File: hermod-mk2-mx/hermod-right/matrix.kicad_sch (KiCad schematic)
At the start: 84 parts

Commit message: UPdated Hermod Mk 2 to have ks33 and choc v2 footprints
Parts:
- CH1, CH10, CH11, CH12, CH13, CH15, CH16, CH17, CH18, CH19, CH2, CH20, CH22, CH23, CH24, CH25, CH26, CH27, CH29, CH3, CH30, CH31, CH32, CH33, CH34, CH39, CH4, CH40, CH41, CH42, CH5, CH6, CH8, CH9: footprint Gateron_KS33_Hotswap:Gateron-KS33-Hotswap-1U -> ModHob:KS33_Choc-v2_HS_1U
- CH14, CH21, CH28, CH35, CH36, CH37, CH38, CH7: footprint Gateron_KS33_Hotswap:Gateron-KS33-Hotswap-1.5U -> ModHob:KS33_Choc-v2_HS_1.5U
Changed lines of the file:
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@@
 			)
 		)
-		(property "Footprint" "Gateron_KS33_Hotswap:Gateron-KS33-Hotswap-1.5U"
+		(property "Footprint" "ModHob:KS33_Choc-v2_HS_1.5U"
 			(at 247.65 162.56 0)
 			(effects
@@
 			)
 		)
-		(property "Footprint" "Gateron_KS33_Hotswap:Gateron-KS33-Hotswap-1U"
+		(property "Footprint" "ModHob:KS33_Choc-v2_HS_1U"
 			(at 212.09 186.69 0)
 			(effects
@@
 			)
 		)
-		(property "Footprint" "Gateron_KS33_Hotswap:Gateron-KS33-Hotswap-1U"
+		(property "Footprint" "ModHob:KS33_Choc-v2_HS_1U"
 			(at 229.87 186.69 0)
 			(effects
@@
 			)
 		)
-		(property "Footprint" "Gateron_KS33_Hotswap:Gateron-KS33-Hotswap-1U"
+		(property "Footprint" "ModHob:KS33_Choc-v2_HS_1U"
 			(at 158.75 95.25 0)
 			(effects
@@
 			)
 		)
-		(property "Footprint" "Gateron_KS33_Hotswap:Gateron-KS33-Hotswap-1U"
+		(property "Footprint" "ModHob:KS33_Choc-v2_HS_1U"
 			(at 212.09 118.11 0)
 			(effects
@@
 			)
 		)
-		(property "Footprint" "Gateron_KS33_Hotswap:Gateron-KS33-Hotswap-1U"
+		(property "Footprint" "ModHob:KS33_Choc-v2_HS_1U"
 			(at 229.87 95.25 0)
 			(effects
@@
 			)
 		)
-		(property "Footprint" "Gateron_KS33_Hotswap:Gateron-KS33-Hotswap-1U"
+		(property "Footprint" "ModHob:KS33_Choc-v2_HS_1U"
 			(at 158.75 139.7 0)
 			(effects
@@
 			)
 		)
-		(property "Footprint" "Gateron_KS33_Hotswap:Gateron-KS33-Hotswap-1U"
+		(property "Footprint" "ModHob:KS33_Choc-v2_HS_1U"
 			(at 158.75 162.56 0)
 			(effects
@@
 			)
 		)
-		(property "Footprint" "Gateron_KS33_Hotswap:Gateron-KS33-Hotswap-1U"
+		(property "Footprint" "ModHob:KS33_Choc-v2_HS_1U"
 			(at 194.31 72.39 0)
 			(effects
@@
 			)
 		)
-		(property "Footprint" "Gateron_KS33_Hotswap:Gateron-KS33-Hotswap-1U"
+		(property "Footprint" "ModHob:KS33_Choc-v2_HS_1U"
 			(at 140.97 139.7 0)
 			(effects
@@
 			)
 		)
-		(property "Footprint" "Gateron_KS33_Hotswap:Gateron-KS33-Hotswap-1.5U"
+		(property "Footprint" "ModHob:KS33_Choc-v2_HS_1.5U"
 			(at 247.65 118.11 0)
 			(effects
@@
 			)
 		)
-		(property "Footprint" "Gateron_KS33_Hotswap:Gateron-KS33-Hotswap-1U"
+		(property "Footprint" "ModHob:KS33_Choc-v2_HS_1U"
 			(at 176.53 139.7 0)
 			(effects
@@
 			)
 		)
-		(property "Footprint" "Gateron_KS33_Hotswap:Gateron-KS33-Hotswap-1U"
+		(property "Footprint" "ModHob:KS33_Choc-v2_HS_1U"
 			(at 229.87 162.56 0)
 			(effects
@@
 			)
 		)
-		(property "Footprint" "Gateron_KS33_Hotswap:Gateron-KS33-Hotswap-1U"
+		(property "Footprint" "ModHob:KS33_Choc-v2_HS_1U"
 			(at 158.75 118.11 0)
 			(effects
@@
 			)
 		)
-		(property "Footprint" "Gateron_KS33_Hotswap:Gateron-KS33-Hotswap-1U"
+		(property "Footprint" "ModHob:KS33_Choc-v2_HS_1U"
 			(at 140.97 162.56 0)
 			(effects
@@
 			)
 		)
-		(property "Footprint" "Gateron_KS33_Hotswap:Gateron-KS33-Hotswap-1U"
+		(property "Footprint" "ModHob:KS33_Choc-v2_HS_1U"
 			(at 229.87 72.39 0)
 			(effects
@@
 			)
 		)
-		(property "Footprint" "Gateron_KS33_Hotswap:Gateron-KS33-Hotswap-1.5U"
+		(property "Footprint" "ModHob:KS33_Choc-v2_HS_1.5U"
 			(at 176.53 186.69 0)
 			(effects
@@
 			)
 		)
-		(property "Footprint" "Gateron_KS33_Hotswap:Gateron-KS33-Hotswap-1.5U"
+		(property "Footprint" "ModHob:KS33_Choc-v2_HS_1.5U"
 			(at 247.65 72.39 0)
 			(effects
@@
 			)
 		)
-		(property "Footprint" "Gateron_KS33_Hotswap:Gateron-KS33-Hotswap-1.5U"
+		(property "Footprint" "ModHob:KS33_Choc-v2_HS_1.5U"
 			(at 140.97 186.69 0)
 			(effects
@@
 			)
 		)
-		(property "Footprint" "Gateron_KS33_Hotswap:Gateron-KS33-Hotswap-1U"
+		(property "Footprint" "ModHob:KS33_Choc-v2_HS_1U"
 			(at 176.53 118.11 0)
 			(effects
@@
 			)
 		)
-		(property "Footprint" "Gateron_KS33_Hotswap:Gateron-KS33-Hotswap-1U"
+		(property "Footprint" "ModHob:KS33_Choc-v2_HS_1U"
 			(at 140.97 72.39 0)
 			(effects
@@
 			)
 		)
-		(property "Footprint" "Gateron_KS33_Hotswap:Gateron-KS33-Hotswap-1U"
+		(property "Footprint" "ModHob:KS33_Choc-v2_HS_1U"
 			(at 194.31 162.56 0)
 			(effects
@@
 			)
 		)
-		(property "Footprint" "Gateron_KS33_Hotswap:Gateron-KS33-Hotswap-1U"
+		(property "Footprint" "ModHob:KS33_Choc-v2_HS_1U"
 			(at 194.31 118.11 0)
 			(effects
@@
 			)
 		)
-		(property "Footprint" "Gateron_KS33_Hotswap:Gateron-KS33-Hotswap-1U"
+		(property "Footprint" "ModHob:KS33_Choc-v2_HS_1U"
 			(at 176.53 95.25 0)
 			(effects
@@
 			)
 		)
-		(property "Footprint" "Gateron_KS33_Hotswap:Gateron-KS33-Hotswap-1U"
+		(property "Footprint" "ModHob:KS33_Choc-v2_HS_1U"
 			(at 229.87 139.7 0)
 			(effects
@@
 			)
 		)
-		(property "Footprint" "Gateron_KS33_Hotswap:Gateron-KS33-Hotswap-1U"
+		(property "Footprint" "ModHob:KS33_Choc-v2_HS_1U"
 			(at 194.31 139.7 0)
 			(effects
@@
 			)
 		)
-		(property "Footprint" "Gateron_KS33_Hotswap:Gateron-KS33-Hotswap-1U"
+		(property "Footprint" "ModHob:KS33_Choc-v2_HS_1U"
 			(at 140.97 95.25 0)
 			(effects
@@
 			)
 		)
-		(property "Footprint" "Gateron_KS33_Hotswap:Gateron-KS33-Hotswap-1U"
+		(property "Footprint" "ModHob:KS33_Choc-v2_HS_1U"
 			(at 158.75 72.39 0)
 			(effects
@@
 			)
 		)
-		(property "Footprint" "Gateron_KS33_Hotswap:Gateron-KS33-Hotswap-1U"
+		(property "Footprint" "ModHob:KS33_Choc-v2_HS_1U"
 			(at 229.87 118.11 0)
 			(effects
@@
 			)
 		)
-		(property "Footprint" "Gateron_KS33_Hotswap:Gateron-KS33-Hotswap-1U"
+		(property "Footprint" "ModHob:KS33_Choc-v2_HS_1U"
 			(at 212.09 72.39 0)
 			(effects
@@
 			)
 		)
-		(property "Footprint" "Gateron_KS33_Hotswap:Gateron-KS33-Hotswap-1.5U"
+		(property "Footprint" "ModHob:KS33_Choc-v2_HS_1.5U"
 			(at 158.75 186.69 0)
 			(effects
@@
 			)
 		)
-		(property "Footprint" "Gateron_KS33_Hotswap:Gateron-KS33-Hotswap-1.5U"
+		(property "Footprint" "ModHob:KS33_Choc-v2_HS_1.5U"
 			(at 247.65 139.7 0)
 			(effects
@@
 			)
 		)
-		(property "Footprint" "Gateron_KS33_Hotswap:Gateron-KS33-Hotswap-1U"
+		(property "Footprint" "ModHob:KS33_Choc-v2_HS_1U"
 			(at 140.97 118.11 0)
 			(effects
@@
 			)
 		)
-		(property "Footprint" "Gateron_KS33_Hotswap:Gateron-KS33-Hotswap-1U"
+		(property "Footprint" "ModHob:KS33_Choc-v2_HS_1U"
 			(at 212.09 162.56 0)
 			(effects
@@
 			)
 		)
-		(property "Footprint" "Gateron_KS33_Hotswap:Gateron-KS33-Hotswap-1U"
+		(property "Footprint" "ModHob:KS33_Choc-v2_HS_1U"
 			(at 247.65 186.69 0)
 			(effects
@@
 			)
 		)
-		(property "Footprint" "Gateron_KS33_Hotswap:Gateron-KS33-Hotswap-1U"
+		(property "Footprint" "ModHob:KS33_Choc-v2_HS_1U"
 			(at 176.53 72.39 0)
 			(effects
@@
 			)
 		)
-		(property "Footprint" "Gateron_KS33_Hotswap:Gateron-KS33-Hotswap-1U"
+		(property "Footprint" "ModHob:KS33_Choc-v2_HS_1U"
 			(at 212.09 139.7 0)
 			(effects
@@
 			)
 		)
-		(property "Footprint" "Gateron_KS33_Hotswap:Gateron-KS33-Hotswap-1U"
+		(property "Footprint" "ModHob:KS33_Choc-v2_HS_1U"
 			(at 194.31 186.69 0)
 			(effects
@@
 			)
 		)
-		(property "Footprint" "Gateron_KS33_Hotswap:Gateron-KS33-Hotswap-1.5U"
+		(property "Footprint" "ModHob:KS33_Choc-v2_HS_1.5U"
 			(at 247.65 95.25 0)
 			(effects
@@
 			)
 		)
-		(property "Footprint" "Gateron_KS33_Hotswap:Gateron-KS33-Hotswap-1U"
+		(property "Footprint" "ModHob:KS33_Choc-v2_HS_1U"
 			(at 194.31 95.25 0)
 			(effects
@@
 			)
 		)
-		(property "Footprint" "Gateron_KS33_Hotswap:Gateron-KS33-Hotswap-1U"
+		(property "Footprint" "ModHob:KS33_Choc-v2_HS_1U"
 			(at 176.53 162.56 0)
 			(effects
@@
 			)
 		)
-		(property "Footprint" "Gateron_KS33_Hotswap:Gateron-KS33-Hotswap-1U"
+		(property "Footprint" "ModHob:KS33_Choc-v2_HS_1U"
 			(at 212.09 95.25 0)
 			(effects

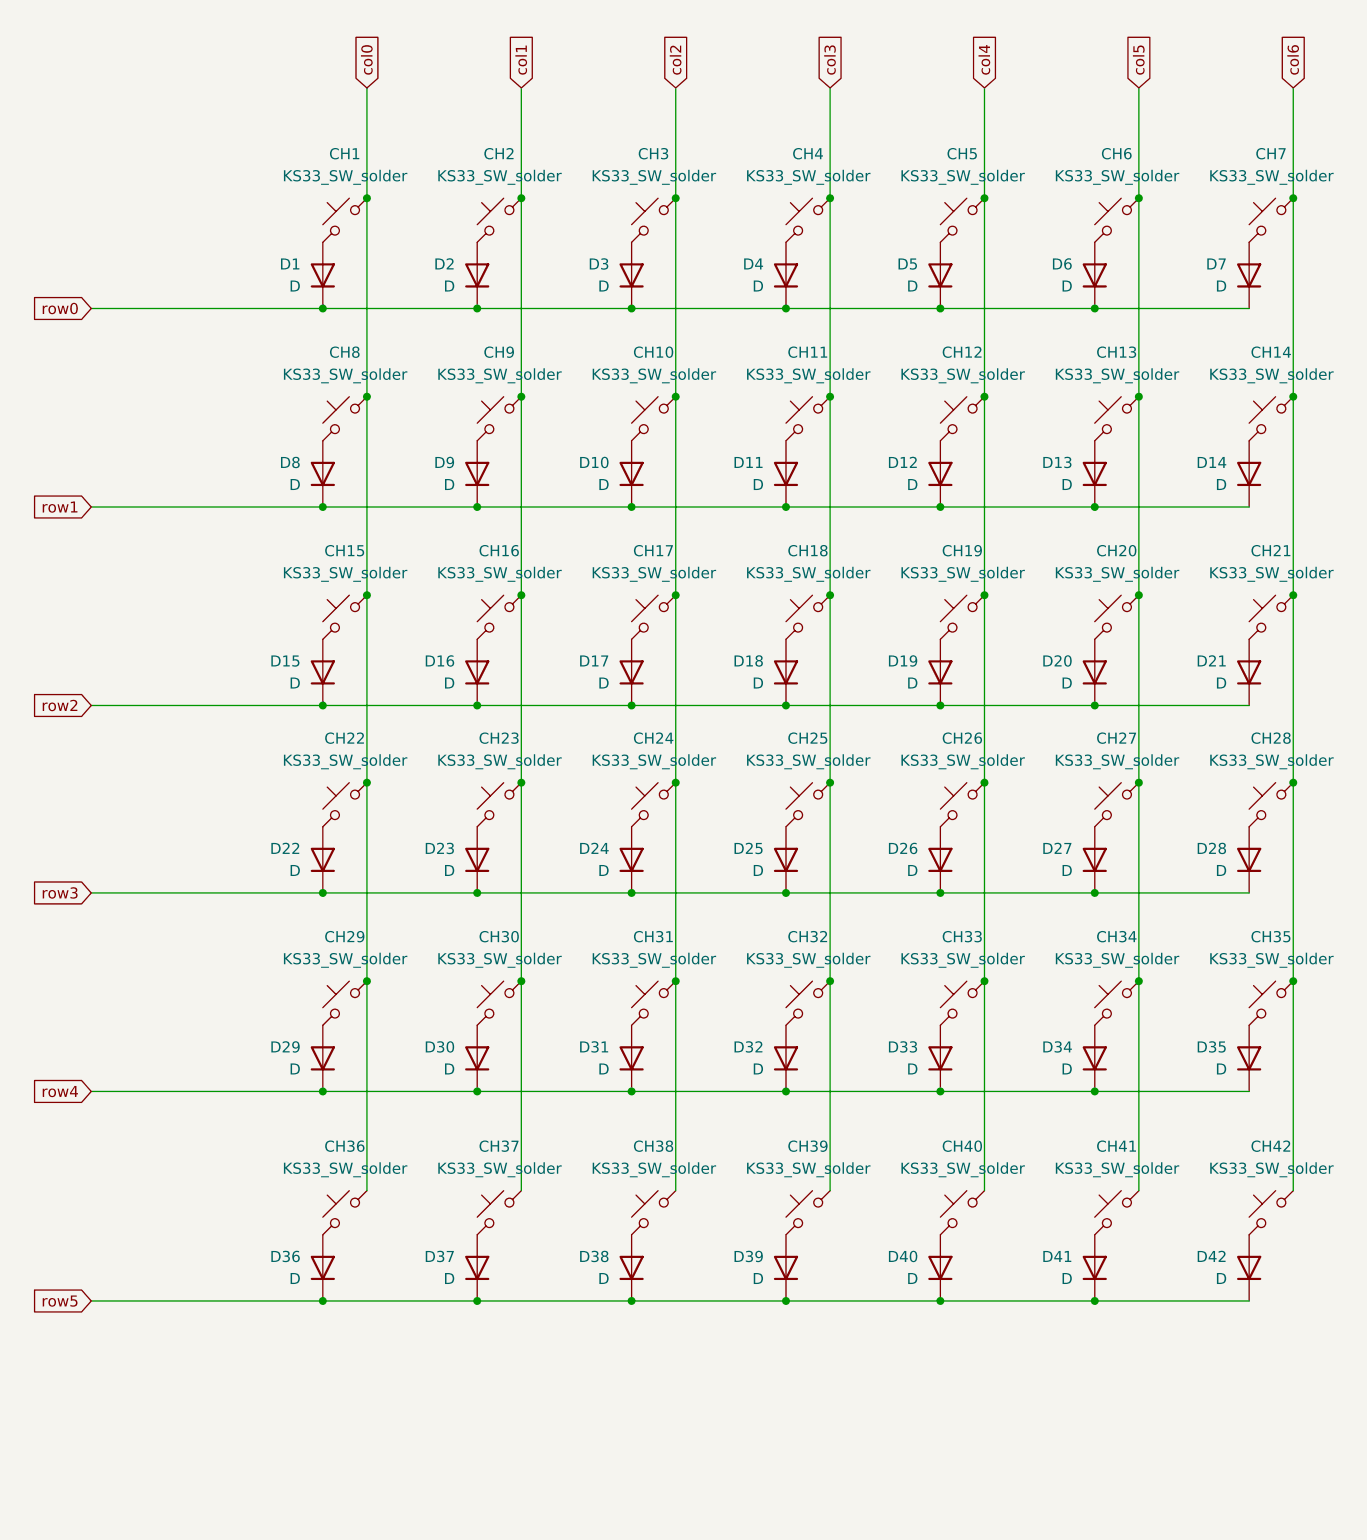
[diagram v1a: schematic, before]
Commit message: Added switches to hermod 3 and updated mist thumb spacing
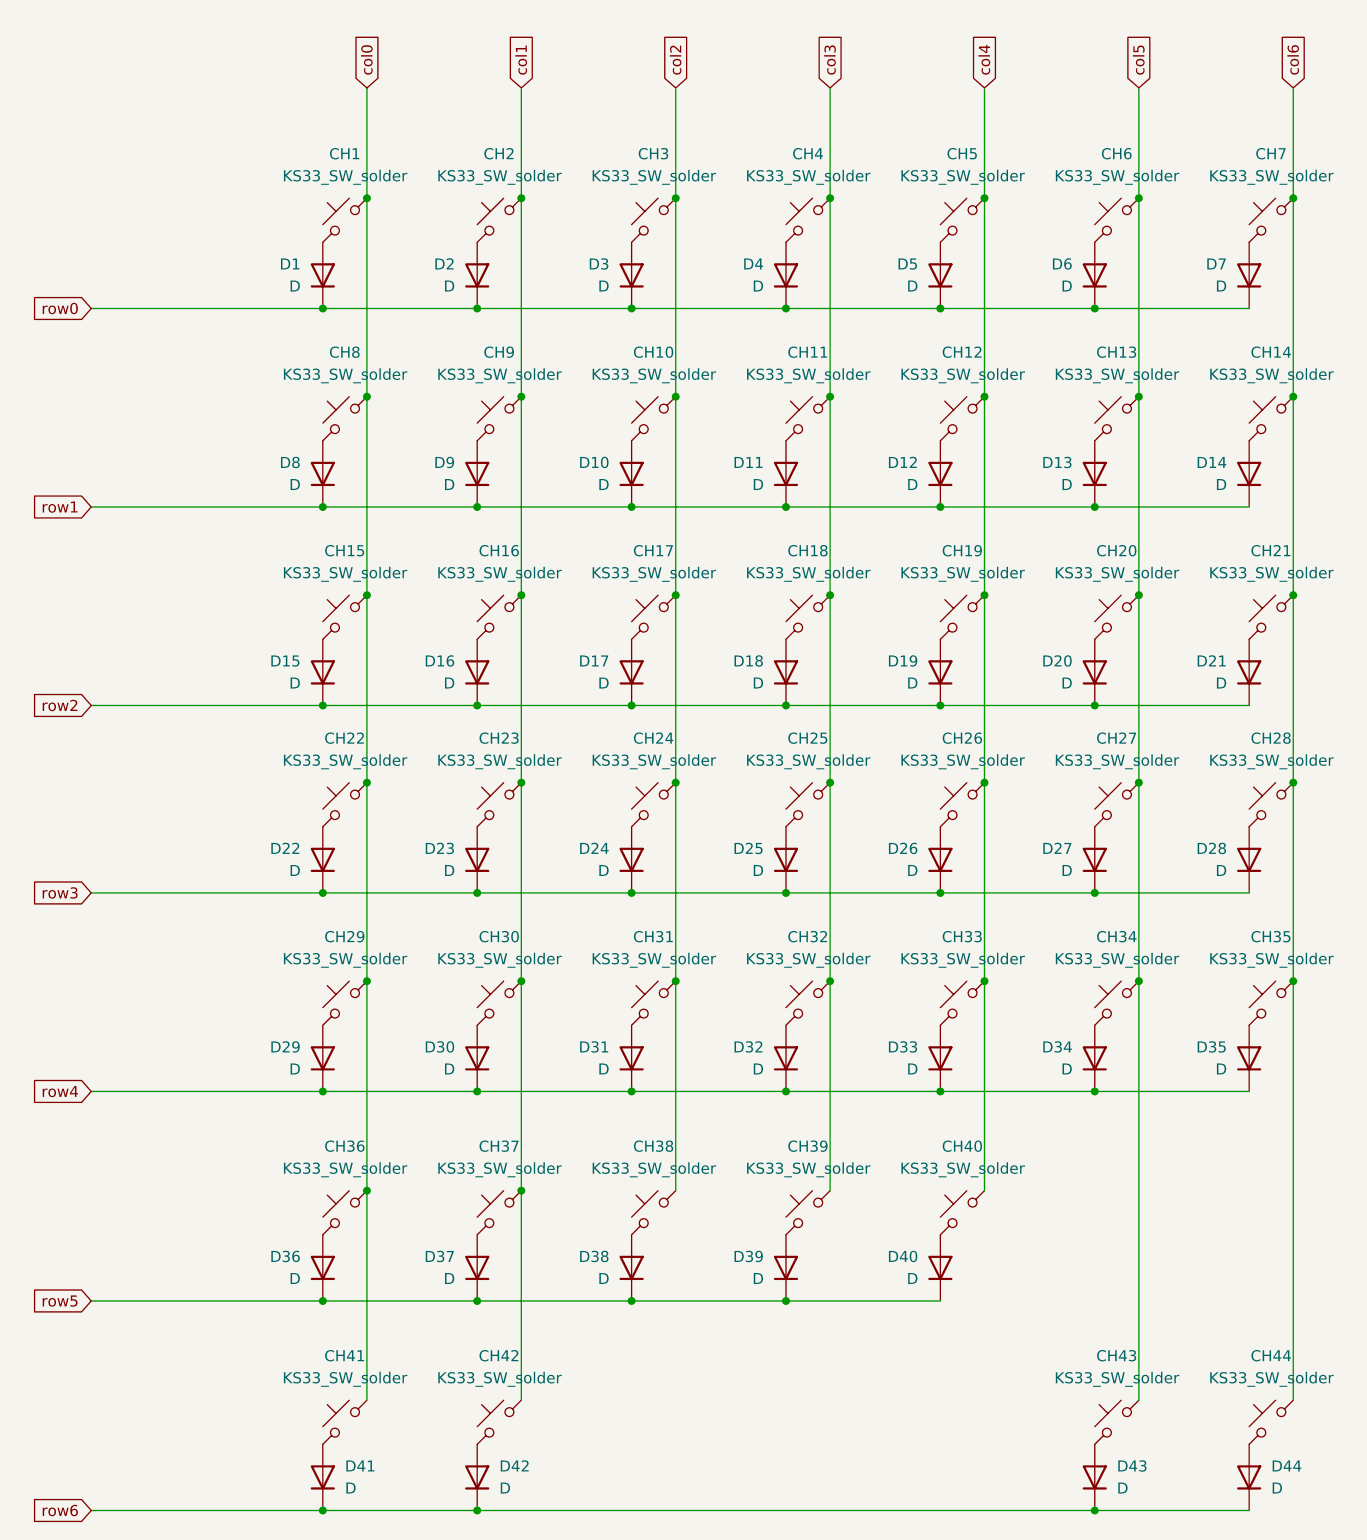
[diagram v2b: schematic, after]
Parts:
- added CH43: KS33_SW_solder, ModHob:KS33_Choc-v2_HS_1.5U, symbol PCM_marbastlib-choc:choc_v1_SW_HS_CPG135001S30
- added CH44: KS33_SW_solder, ModHob:KS33_Choc-v2_HS_1U, symbol PCM_marbastlib-choc:choc_v1_SW_HS_CPG135001S30
- added D43, D44: D, Diode_SMD:D_SOD-123, symbol Device:D
- CH41, CH42: footprint ModHob:KS33_Choc-v2_HS_1U -> ModHob:KS33_Choc-v2_HS_1.5U
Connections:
- net col0: now also CH41.1
- net col1: now also CH42.1
- net col5: now also CH43.1; no longer CH41.1
- net col6: now also CH44.1; no longer CH42.1
- net row5: no longer D41.1 (K), D42.1 (K)
- new net: CH43.2, D43.2 (A)
- new net: CH44.2, D44.2 (A)
- new net row6: D41.1 (K), D42.1 (K), D43.1 (K), D44.1 (K)

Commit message: Fixed spacing issues
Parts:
- CH36, CH37, CH41, CH42, CH43: footprint ModHob:KS33_Choc-v2_HS_1.5U -> ModHob:KS33_Choc-v2_HS_1U
- CH39, CH40: footprint ModHob:KS33_Choc-v2_HS_1U -> ModHob:KS33_Choc-v2_HS_1.5U
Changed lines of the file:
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@@
 			)
 		)
-		(property "Footprint" "ModHob:KS33_Choc-v2_HS_1.5U"
+		(property "Footprint" "ModHob:KS33_Choc-v2_HS_1U"
 			(at 229.87 210.82 0)
 			(effects
@@
 			)
 		)
-		(property "Footprint" "ModHob:KS33_Choc-v2_HS_1U"
+		(property "Footprint" "ModHob:KS33_Choc-v2_HS_1.5U"
 			(at 212.09 186.69 0)
 			(effects
@@
 			)
 		)
-		(property "Footprint" "ModHob:KS33_Choc-v2_HS_1.5U"
+		(property "Footprint" "ModHob:KS33_Choc-v2_HS_1U"
 			(at 140.97 210.82 0)
 			(effects
@@
 			)
 		)
-		(property "Footprint" "ModHob:KS33_Choc-v2_HS_1.5U"
+		(property "Footprint" "ModHob:KS33_Choc-v2_HS_1U"
 			(at 158.75 210.82 0)
 			(effects
@@
 			)
 		)
-		(property "Footprint" "ModHob:KS33_Choc-v2_HS_1.5U"
+		(property "Footprint" "ModHob:KS33_Choc-v2_HS_1U"
 			(at 140.97 186.69 0)
 			(effects
@@
 			)
 		)
-		(property "Footprint" "ModHob:KS33_Choc-v2_HS_1.5U"
+		(property "Footprint" "ModHob:KS33_Choc-v2_HS_1U"
 			(at 158.75 186.69 0)
 			(effects
@@
 			)
 		)
-		(property "Footprint" "ModHob:KS33_Choc-v2_HS_1U"
+		(property "Footprint" "ModHob:KS33_Choc-v2_HS_1.5U"
 			(at 194.31 186.69 0)
 			(effects
